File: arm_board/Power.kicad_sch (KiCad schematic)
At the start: 16 parts, among them J3 Molex_Megafit_02, J4 Molex_Megafit_02, U4 AP63205WU

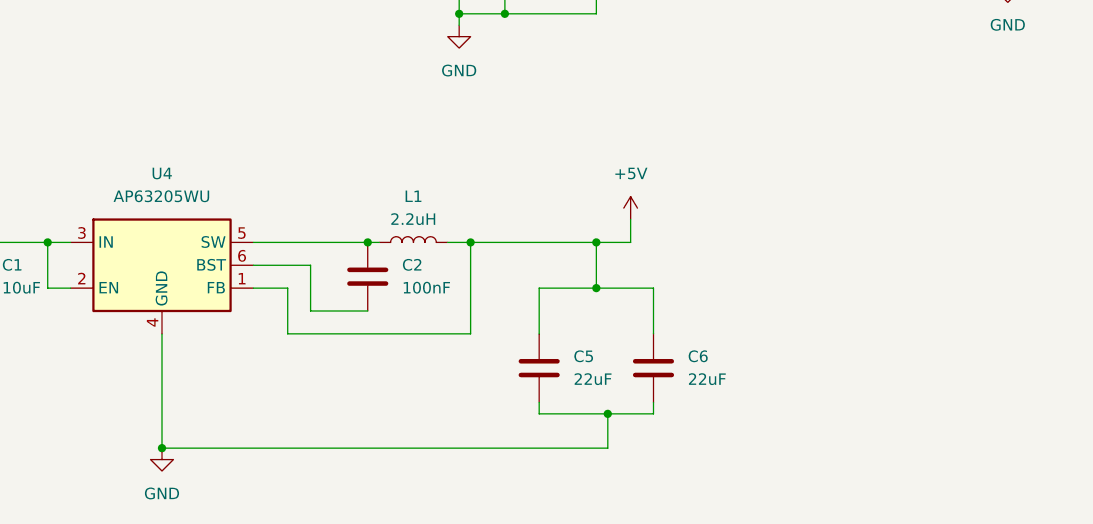
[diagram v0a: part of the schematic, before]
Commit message: Fixed hierarchal sheets / Rove Node
Got rid of unneeded hierarchal sheets and fixed MCU pins.
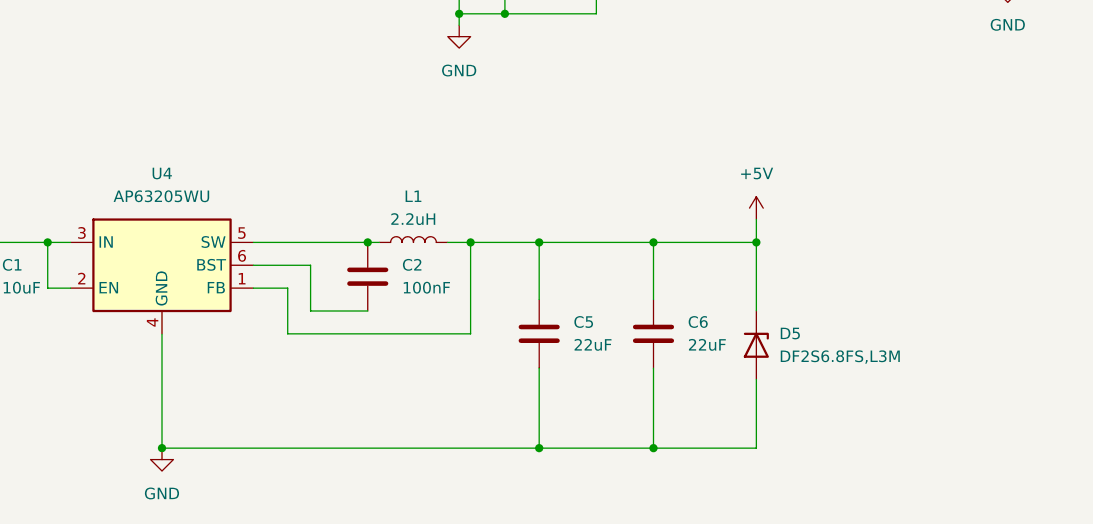
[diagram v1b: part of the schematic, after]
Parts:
- added D5: DF2S6.8FS,L3M, Package_DIP:DIP-40_W15.24mm, symbol Device:D_Zener
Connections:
- net +5V: now also D5.1 (K)
- net GND: now also D5.2 (A)
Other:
- moved on the sheet: C5, C6

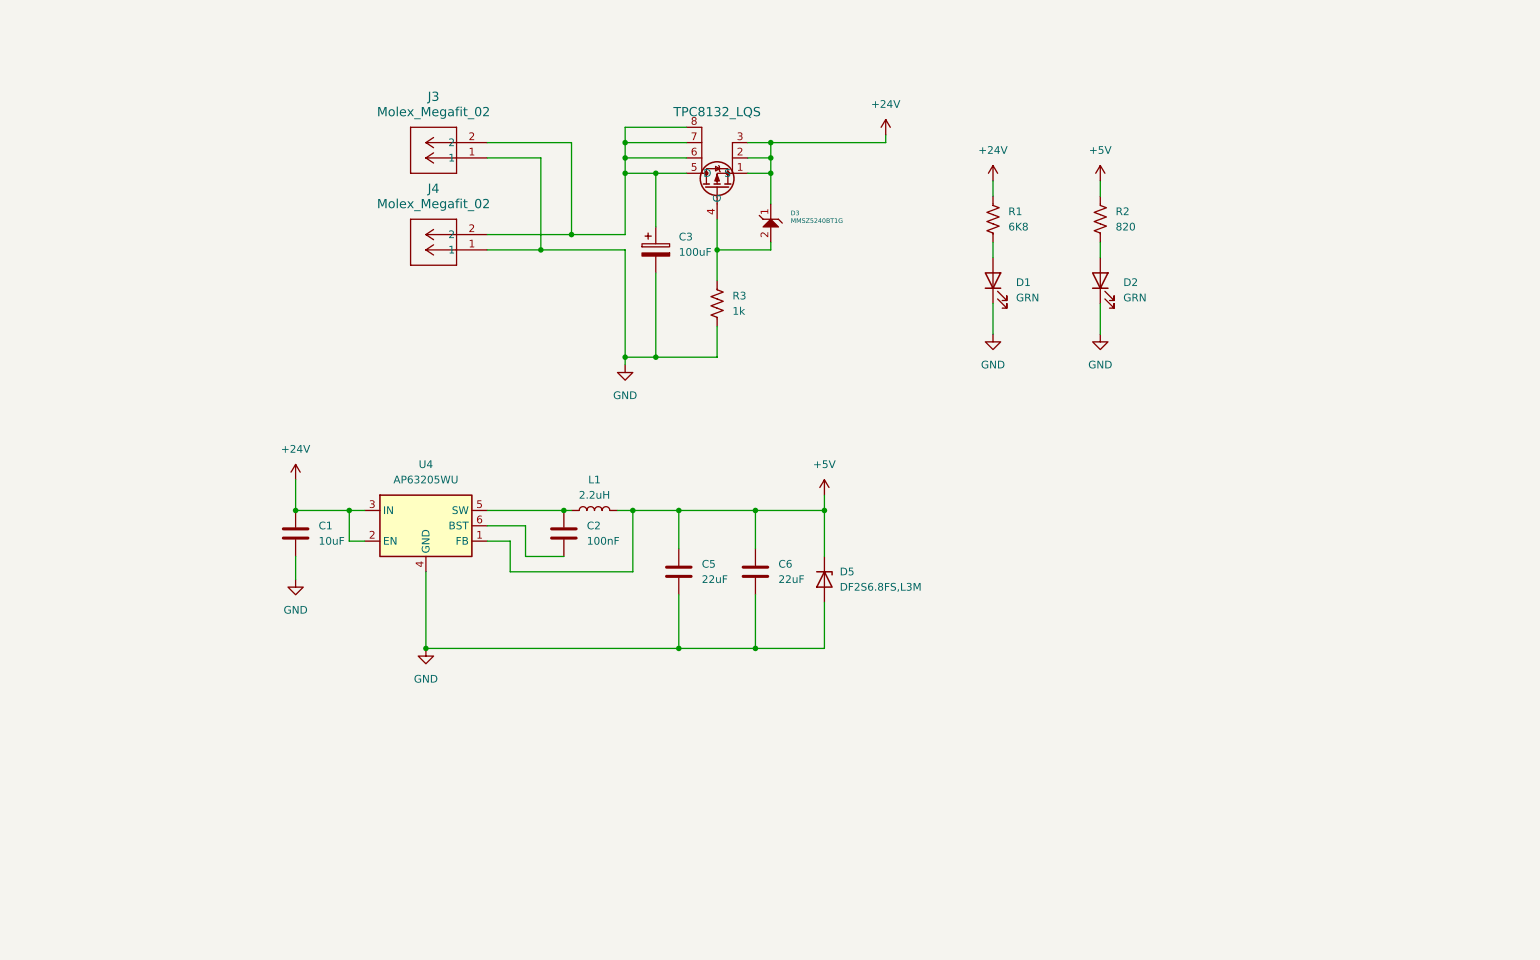
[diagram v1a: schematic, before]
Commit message: schematic meeting changes
We fixed the changes from the schematic review
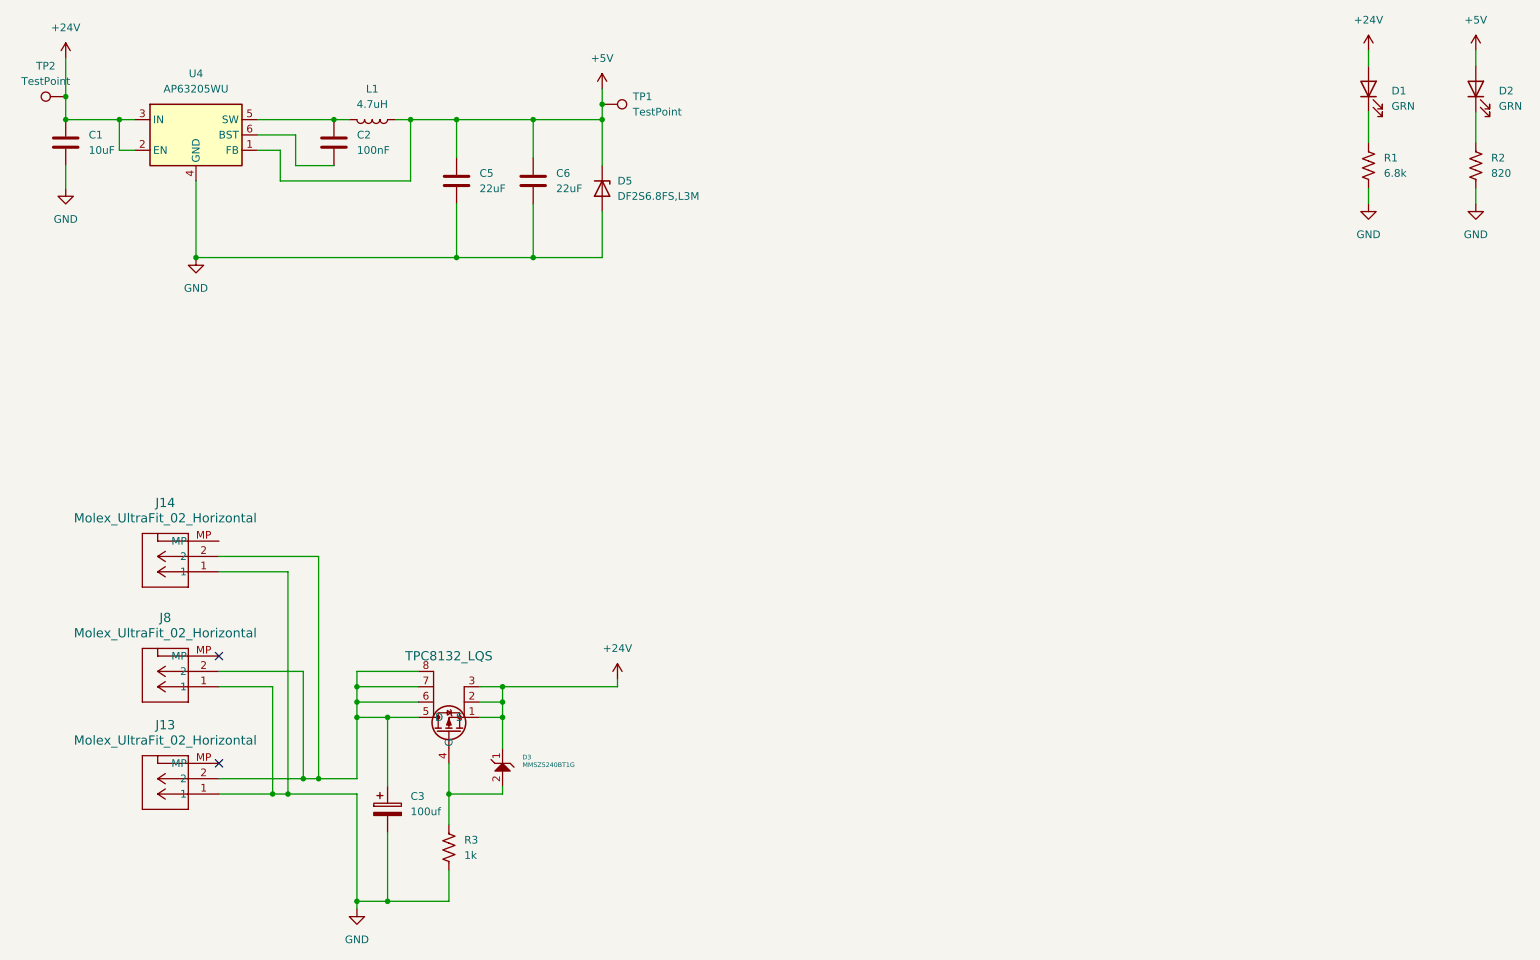
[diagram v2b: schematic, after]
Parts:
- removed J3, J4: Molex_Megafit_02, MRDT_Connectors:MOLEX_MegaFit_02_Horizontal, symbol MRDT_Connectors:Molex_Megafit_02
- added J13, J14, J8: Molex_UltraFit_02_Horizontal, MRDT_Connectors:MOLEX_UltraFit_02_Horizontal, symbol MRDT_Connectors:Molex_UltraFit_02_Horizontal
- added TP1, TP2: TestPoint, Relay_THT:Relay_DPDT_Schrack-RT2-FormC_RM5mm, symbol Connector:TestPoint
- C3: value 100uF -> 100uf; footprint Capacitor_THT:CP_Radial_D6.3mm_P2.50mm -> Capacitor_SMD:C_0603_1608Metric_Pad1.08x0.95mm_HandSolder
- L1: value 2.2uH -> 4.7uH; footprint Inductor_SMD:L_0603_1608Metric_Pad1.05x0.95mm_HandSolder -> footprints:IND_DFE322520FD-4R7M=P2_MUR
- R1: value 6K8 -> 6.8k
- R3: footprint Resistor_SMD:R_0603_1608Metric_Pad0.98x0.95mm_HandSolder -> Package_LCC:PLCC-84_29.3x29.3mm_P1.27mm
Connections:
- net +24V: now also D1.2 (A), TP2.1; no longer R1.1
- net +5V: now also D2.2 (A), L1.1, TP1.1; no longer L1.2, R2.1
- net GND: now also R1.2, R2.2, J13.1, J14.1, J8.1; no longer D1.1 (K), D2.1 (K)
- net at C2.1, U4.5 (SW): now also L1.2; no longer L1.1
- net at C3.1, MOSFET1.5 (D), MOSFET1.6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: now also J13.2, J14.2, J8.2
- new net: D1.1 (K), R1.1
- new net: D2.1 (K), R2.1
- no-connect marks 0 -> 2
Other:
- moved on the sheet: C1, C2, C5, C6, D1, D2, D3, D5, R1, R2, U4

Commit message: updated the button footprints
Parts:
- R3: footprint Package_LCC:PLCC-84_29.3x29.3mm_P1.27mm -> Resistor_SMD:R_0603_1608Metric_Pad0.98x0.95mm_HandSolder
- TP1: footprint Relay_THT:Relay_DPDT_Schrack-RT2-FormC_RM5mm -> TestPoint:TestPoint_Pad_1.5x1.5mm
- TP2: footprint Relay_THT:Relay_DPDT_Schrack-RT2-FormC_RM5mm -> TestPoint:TestPoint_Pad_1.5x1.5mm; now left out of the parts list
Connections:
- no-connect marks 2 -> 3

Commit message: updated footprints
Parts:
- D5: footprint Package_DIP:DIP-40_W15.24mm -> Diode_SMD:D_SOD-923

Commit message: edited footprints and layout
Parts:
- D5: footprint Diode_SMD:D_SOD-923 -> footprints:SOD-323_1P8X1P35_ONS
- J13, J14, J8: footprint MRDT_Connectors:MOLEX_UltraFit_02_Horizontal -> MRDT_Connectors:MOLEX_MegaFit_02_Horizontal

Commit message: pre CDR design
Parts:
- C3: footprint Capacitor_SMD:C_0603_1608Metric_Pad1.08x0.95mm_HandSolder -> Capacitor_THT:CP_Radial_D6.3mm_P2.50mm
